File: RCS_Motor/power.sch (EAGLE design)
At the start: 3 parts, among them M1 SMALL_SERVO

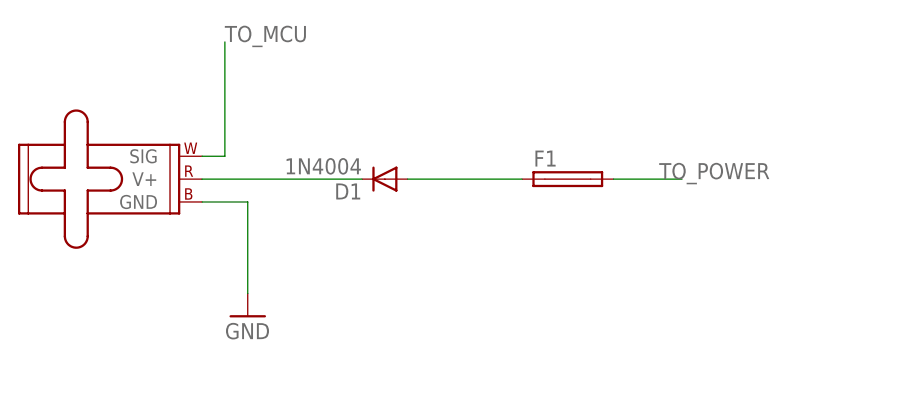
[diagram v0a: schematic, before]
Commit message: Updated/New Schematics
I don't think this updated when I did it on tuesday
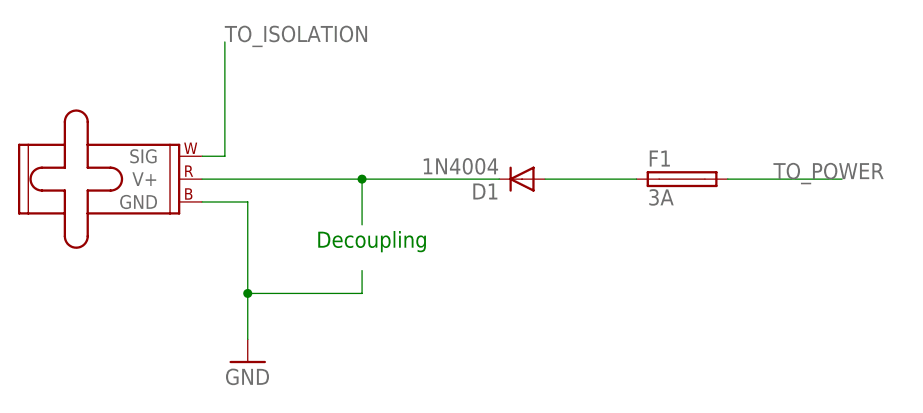
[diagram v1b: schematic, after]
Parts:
- F1: value (none) -> 3A
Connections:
- net TO_MCU renamed TO_ISOLATION
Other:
- note added: "Decoupling"
- moved on the sheet: D1, F1
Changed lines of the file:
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@@
 <parts>
 <part name="M1" library="SparkFun-Electromechanical" deviceset="SMALL_SERVO" device=""/>
-<part name="F1" library="fuse" deviceset="TE5" device=""/>
+<part name="F1" library="fuse" deviceset="TE5" device="" value="3A"/>
 <part name="D1" library="adafruit" deviceset="1N4004" device=""/>
 <part name="GND1" library="SparkFun-Aesthetics" deviceset="GND" device=""/>
@@
 <sheet>
 <plain>
+<text x="10.16" y="58.42" size="1.778" layer="91">Decoupling</text>
 </plain>
 <instances>
 <instance part="M1" gate="G$1" x="-5.08" y="68.58"/>
-<instance part="F1" gate="1" x="38.1" y="66.04"/>
-<instance part="D1" gate="1" x="17.78" y="66.04" rot="R180"/>
-<instance part="GND1" gate="1" x="2.54" y="50.8"/>
+<instance part="F1" gate="1" x="50.8" y="66.04"/>
+<instance part="D1" gate="1" x="33.02" y="66.04" rot="R180"/>
+<instance part="GND1" gate="1" x="2.54" y="45.72"/>
 </instances>
 <busses>
@@
 <wire x1="-2.54" y1="63.5" x2="2.54" y2="63.5" width="0.1524" layer="91"/>
 <wire x1="2.54" y1="63.5" x2="2.54" y2="53.34" width="0.1524" layer="91"/>
+<wire x1="2.54" y1="53.34" x2="2.54" y2="48.26" width="0.1524" layer="91"/>
+<wire x1="15.24" y1="55.88" x2="15.24" y2="53.34" width="0.1524" layer="91"/>
+<wire x1="15.24" y1="53.34" x2="2.54" y2="53.34" width="0.1524" layer="91"/>
+<junction x="2.54" y="53.34"/>
+</segment>
+</net>
+<net name="N$2" class="0">
+<segment>
+<pinref part="D1" gate="1" pin="A"/>
+<pinref part="F1" gate="1" pin="1"/>
+<wire x1="35.56" y1="66.04" x2="45.72" y2="66.04" width="0.1524" layer="91"/>
+</segment>
+</net>
+<net name="TO_POWER" class="0">
+<segment>
+<pinref part="F1" gate="1" pin="2"/>
+<wire x1="55.88" y1="66.04" x2="68.58" y2="66.04" width="0.1524" layer="91"/>
+<label x="60.96" y="66.04" size="1.778" layer="95"/>
+</segment>
+</net>
+<net name="TO_ISOLATION" class="0">
+<segment>
+<pinref part="M1" gate="G$1" pin="SIG"/>
+<wire x1="-2.54" y1="68.58" x2="0" y2="68.58" width="0.1524" layer="91"/>
+<wire x1="0" y1="68.58" x2="0" y2="81.28" width="0.1524" layer="91"/>
+<label x="0" y="81.28" size="1.778" layer="95"/>
 </segment>
 </net>
@@
 <pinref part="D1" gate="1" pin="C"/>
 <wire x1="-2.54" y1="66.04" x2="15.24" y2="66.04" width="0.1524" layer="91"/>
+<wire x1="15.24" y1="66.04" x2="30.48" y2="66.04" width="0.1524" layer="91"/>
+<wire x1="15.24" y1="60.96" x2="15.24" y2="66.04" width="0.1524" layer="91"/>
+<junction x="15.24" y="66.04"/>
 </segment>
 </net>
-<net name="N$2" class="0">
-<segment>
-<pinref part="D1" gate="1" pin="A"/>
-<pinref part="F1" gate="1" pin="1"/>
-<wire x1="20.32" y1="66.04" x2="33.02" y2="66.04" width="0.1524" layer="91"/>
-</segment>
-</net>
-<net name="TO_POWER" class="0">
-<segment>
-<pinref part="F1" gate="1" pin="2"/>
-<wire x1="43.18" y1="66.04" x2="50.8" y2="66.04" width="0.1524" layer="91"/>
-<label x="48.26" y="66.04" size="1.778" layer="95"/>
-</segment>
-</net>
-<net name="TO_MCU" class="0">
-<segment>
-<pinref part="M1" gate="G$1" pin="SIG"/>
-<wire x1="-2.54" y1="68.58" x2="0" y2="68.58" width="0.1524" layer="91"/>
-<wire x1="0" y1="68.58" x2="0" y2="81.28" width="0.1524" layer="91"/>
-<label x="0" y="81.28" size="1.778" layer="95"/>
-</segment>
-</net>
